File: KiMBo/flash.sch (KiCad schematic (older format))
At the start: 31 parts, among them IC1 24LC32AT-I/OT, U1 OSD3358, U5 74LVC1G06, U6 EMMC**G-S100

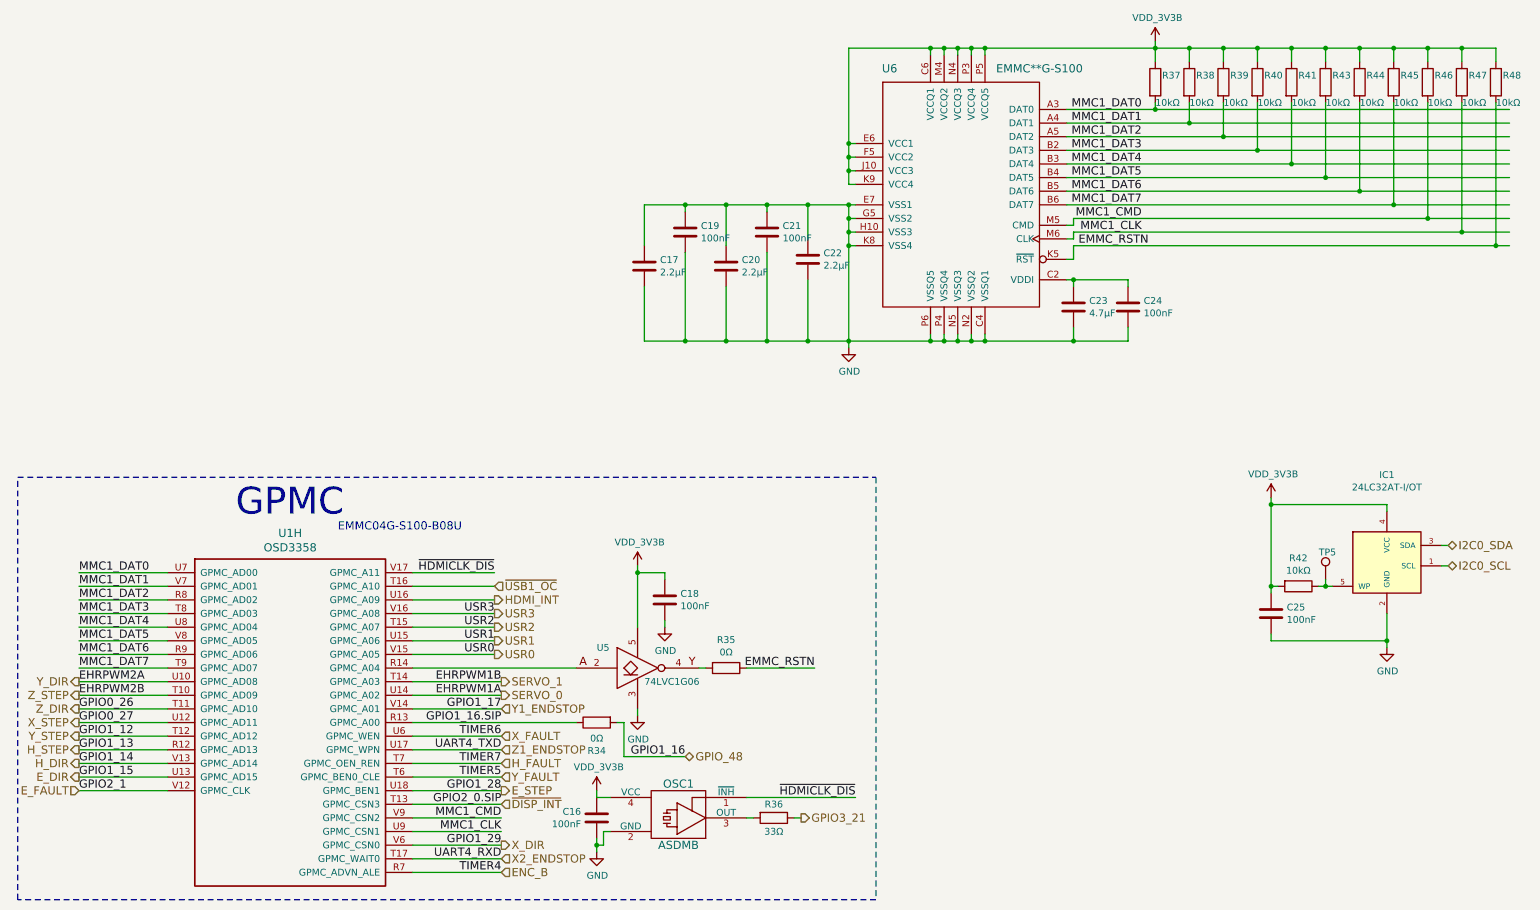
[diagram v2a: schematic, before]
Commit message: Use fixed 5V LM2592HV Buck, include SPI0 header for LCD
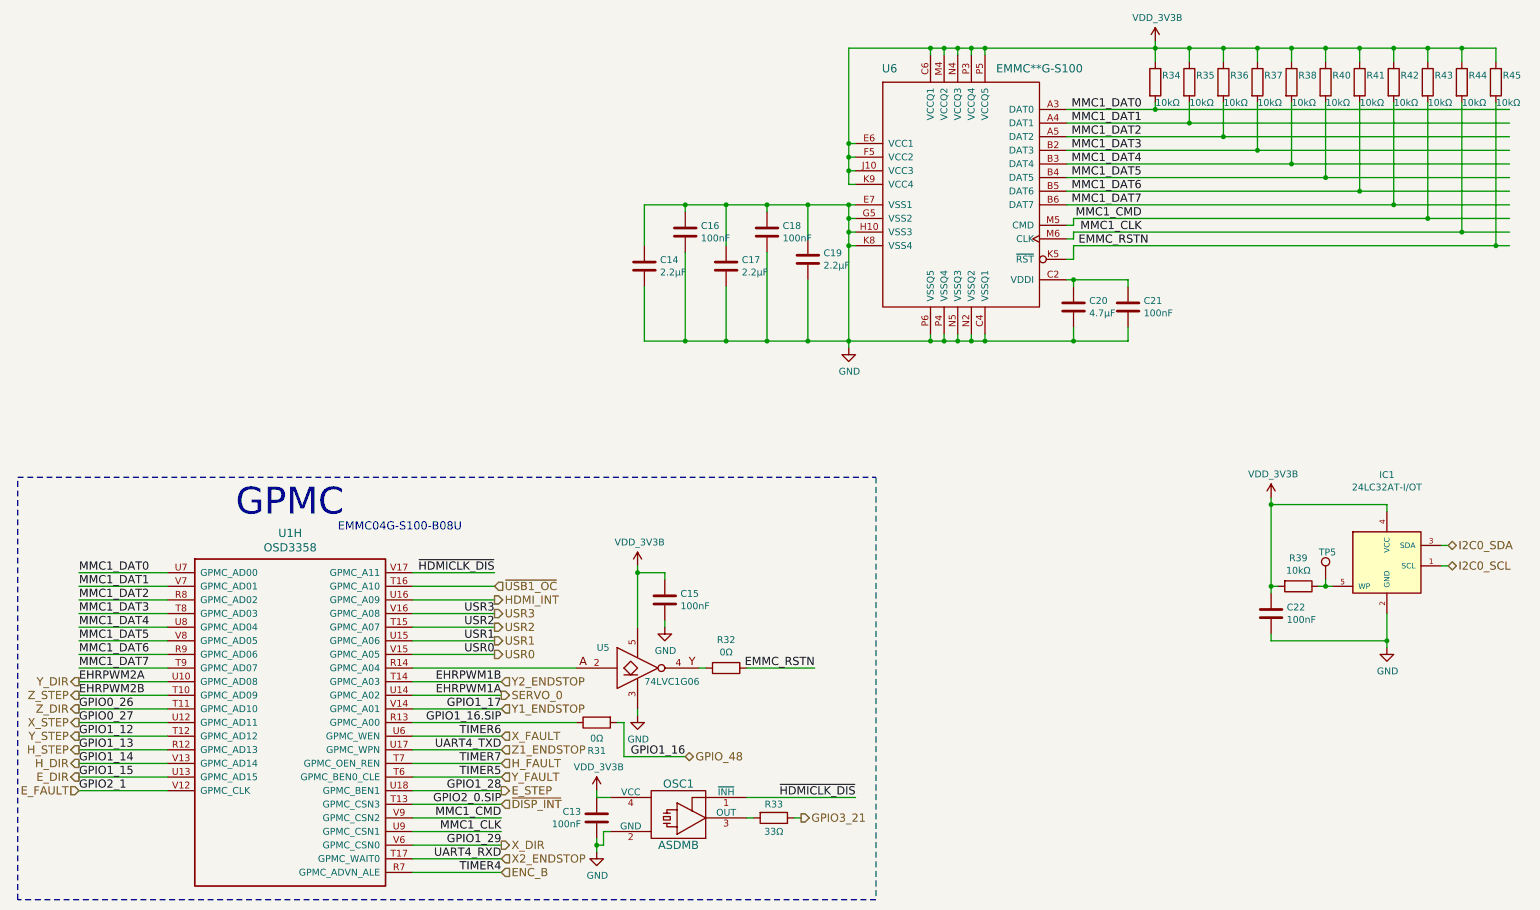
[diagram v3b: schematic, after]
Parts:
- renumbered C16 to C13, C17 to C14, C18 to C15, C19 to C16, C20 to C17, C21 to C18, C22 to C19, C23 to C20, C24 to C21, C25 to C22, R34 to R31, R35 to R32, R36 to R33, R37 to R34, R38 to R35, R39 to R36, R40 to R37, R41 to R38, R42 to R39, R43 to R40, R44 to R41, R45 to R42, R46 to R43, R47 to R44, R48 to R45
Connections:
- net labels added: Y2_ENDSTOP
- net labels removed: SERVO_1
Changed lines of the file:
@@
 $EndDescr
 $Comp
-L R R37
+L R R34
 U 1 1 58938DE0
 P 10550 2900
-F 0 "R37" H 10600 2950 50  0000 L CNN
+F 0 "R34" H 10600 2950 50  0000 L CNN
 F 1 "10kΩ" H 10550 2750 50  0000 L CNN
 F 2 "Resistors_SMD:R_0402" V 10480 2900 50  0001 C CNN
@@
 $EndComp
 $Comp
-L R R38
+L R R35
 U 1 1 58938E26
 P 10800 2900
-F 0 "R38" H 10850 2950 50  0000 L CNN
+F 0 "R35" H 10850 2950 50  0000 L CNN
 F 1 "10kΩ" H 10800 2750 50  0000 L CNN
 F 2 "Resistors_SMD:R_0402" V 10730 2900 50  0001 C CNN
@@
 $EndComp
 $Comp
-L R R39
+L R R36
 U 1 1 58938E51
 P 11050 2900
-F 0 "R39" H 11100 2950 50  0000 L CNN
+F 0 "R36" H 11100 2950 50  0000 L CNN
 F 1 "10kΩ" H 11050 2750 50  0000 L CNN
 F 2 "Resistors_SMD:R_0402" V 10980 2900 50  0001 C CNN
@@
 $EndComp
 $Comp
-L R R40
+L R R37
 U 1 1 58938E75
 P 11300 2900
-F 0 "R40" H 11350 2950 50  0000 L CNN
+F 0 "R37" H 11350 2950 50  0000 L CNN
 F 1 "10kΩ" H 11300 2750 50  0000 L CNN
 F 2 "Resistors_SMD:R_0402" V 11230 2900 50  0001 C CNN
@@
 $EndComp
 $Comp
-L R R41
+L R R38
 U 1 1 58938EA0
 P 11550 2900
-F 0 "R41" H 11600 2950 50  0000 L CNN
+F 0 "R38" H 11600 2950 50  0000 L CNN
 F 1 "10kΩ" H 11550 2750 50  0000 L CNN
 F 2 "Resistors_SMD:R_0402" V 11480 2900 50  0001 C CNN
@@
 $EndComp
 $Comp
-L R R43
+L R R40
 U 1 1 58938F20
 P 11800 2900
-F 0 "R43" H 11850 2950 50  0000 L CNN
+F 0 "R40" H 11850 2950 50  0000 L CNN
 F 1 "10kΩ" H 11800 2750 50  0000 L CNN
 F 2 "Resistors_SMD:R_0402" V 11730 2900 50  0001 C CNN
@@
 	9300 4800 9300 4750
 $Comp
-L R R44
+L R R41
 U 1 1 5893A6C3
 P 12050 2900
-F 0 "R44" H 12100 2950 50  0000 L CNN
+F 0 "R41" H 12100 2950 50  0000 L CNN
 F 1 "10kΩ" H 12050 2750 50  0000 L CNN
 F 2 "Resistors_SMD:R_0402" V 11980 2900 50  0001 C CNN
@@
 $EndComp
 $Comp
-L R R45
+L R R42
 U 1 1 5893A6FB
 P 12300 2900
-F 0 "R45" H 12350 2950 50  0000 L CNN
+F 0 "R42" H 12350 2950 50  0000 L CNN
 F 1 "10kΩ" H 12300 2750 50  0000 L CNN
 F 2 "Resistors_SMD:R_0402" V 12230 2900 50  0001 C CNN
@@
 $EndComp
 $Comp
-L R R46
+L R R43
 U 1 1 5893A736
 P 12550 2900
-F 0 "R46" H 12600 2950 50  0000 L CNN
+F 0 "R43" H 12600 2950 50  0000 L CNN
 F 1 "10kΩ" H 12550 2750 50  0000 L CNN
 F 2 "Resistors_SMD:R_0402" V 12480 2900 50  0001 C CNN
@@
 	10550 3100 10550 3050
 $Comp
-L R R47
+L R R44
 U 1 1 5893AC56
 P 12800 2900
-F 0 "R47" H 12850 2950 50  0000 L CNN
+F 0 "R44" H 12850 2950 50  0000 L CNN
 F 1 "10kΩ" H 12800 2750 50  0000 L CNN
 F 2 "Resistors_SMD:R_0402" V 12730 2900 50  0001 C CNN
@@
 $EndComp
 $Comp
-L R R48
+L R R45
 U 1 1 5893AC8F
 P 13050 2900
-F 0 "R48" H 13100 2950 50  0000 L CNN
+F 0 "R45" H 13100 2950 50  0000 L CNN
 F 1 "10kΩ" H 13050 2750 50  0000 L CNN
 F 2 "Resistors_SMD:R_0402" V 12980 2900 50  0001 C CNN
@@
 Connection ~ 12800 2650
 $Comp
-L GND #PWR097
+L GND #PWR092
 U 1 1 5893C2D6
 P 8300 4850
-F 0 "#PWR097" H 8300 4600 50  0001 C CNN
+F 0 "#PWR092" H 8300 4600 50  0001 C CNN
 F 1 "GND" H 8305 4677 50  0000 C CNN
 F 2 "" H 8300 4850 50  0000 C CNN
@@
 Connection ~ 8300 4800
 $Comp
-L C C23
+L C C20
 U 1 1 5893CB56
 P 9950 4550
-F 0 "C23" H 10065 4596 50  0000 L CNN
+F 0 "C20" H 10065 4596 50  0000 L CNN
 F 1 "4.7μF" H 10065 4505 50  0000 L CNN
 F 2 "Capacitors_SMD:C_0805" H 9950 4550 50  0001 C CNN
@@
 $EndComp
 $Comp
-L C C24
+L C C21
 U 1 1 5893CB95
 P 10350 4550
-F 0 "C24" H 10465 4596 50  0000 L CNN
+F 0 "C21" H 10465 4596 50  0000 L CNN
 F 1 "100nF" H 10465 4505 50  0000 L CNN
 F 2 "Capacitors_SMD:C_0402" H 10350 4550 50  0001 C CNN
@@
 Connection ~ 9950 4350
 $Comp
-L C C22
+L C C19
 U 1 1 5893CF89
 P 8000 4200
-F 0 "C22" H 8115 4246 50  0000 L CNN
+F 0 "C19" H 8115 4246 50  0000 L CNN
 F 1 "2.2μF" H 8115 4155 50  0000 L CNN
 F 2 "Capacitors_SMD:C_0805" H 8000 4200 50  0001 C CNN
@@
 $EndComp
 $Comp
-L C C21
+L C C18
 U 1 1 5893D253
 P 7700 4000
-F 0 "C21" H 7815 4046 50  0000 L CNN
+F 0 "C18" H 7815 4046 50  0000 L CNN
 F 1 "100nF" H 7815 3955 50  0000 L CNN
 F 2 "Capacitors_SMD:C_0402" H 7700 4000 50  0001 C CNN
@@
 $EndComp
 $Comp
-L C C20
+L C C17
 U 1 1 5893D333
 P 7400 4250
-F 0 "C20" H 7515 4296 50  0000 L CNN
+F 0 "C17" H 7515 4296 50  0000 L CNN
 F 1 "2.2μF" H 7515 4205 50  0000 L CNN
 F 2 "Capacitors_SMD:C_0805" H 7400 4250 50  0001 C CNN
@@
 $EndComp
 $Comp
-L C C19
+L C C16
 U 1 1 5893D48C
 P 7100 4000
-F 0 "C19" H 7215 4046 50  0000 L CNN
+F 0 "C16" H 7215 4046 50  0000 L CNN
 F 1 "100nF" H 7215 3955 50  0000 L CNN
 F 2 "Capacitors_SMD:C_0402" H 7100 4000 50  0001 C CNN
@@
 $EndComp
 $Comp
-L C C17
+L C C14
 U 1 1 5893D4EE
 P 6800 4250
-F 0 "C17" H 6915 4296 50  0000 L CNN
+F 0 "C14" H 6915 4296 50  0000 L CNN
 F 1 "2.2μF" H 6915 4205 50  0000 L CNN
 F 2 "Capacitors_SMD:C_0805" H 6800 4250 50  0001 C CNN
@@
 $EndComp
 $Comp
-L R R42
+L R R39
 U 1 1 589CA43D
 P 11600 6600
-F 0 "R42" V 11393 6600 50  0000 C CNN
+F 0 "R39" V 11393 6600 50  0000 C CNN
 F 1 "10kΩ" V 11484 6600 50  0000 C CNN
 F 2 "Resistors_SMD:R_0402" V 11530 6600 50  0001 C CNN
@@
 	11400 6600 11450 6600
 $Comp
-L C C25
+L C C22
 U 1 1 589CA9AC
 P 11400 6800
-F 0 "C25" H 11515 6846 50  0000 L CNN
+F 0 "C22" H 11515 6846 50  0000 L CNN
 F 1 "100nF" H 11515 6755 50  0000 L CNN
 F 2 "Capacitors_SMD:C_0402" H 11400 6800 50  0001 C CNN
@@
 	11400 7000 11400 6950
 $Comp
-L GND #PWR098
+L GND #PWR093
 U 1 1 589CAA98
 P 12250 7050
-F 0 "#PWR098" H 12250 6800 50  0001 C CNN
+F 0 "#PWR093" H 12250 6800 50  0001 C CNN
 F 1 "GND" H 12255 6877 50  0000 C CNN
 F 2 "" H 12250 7050 50  0000 C CNN
@@
 GPIO1_16.SIP
 $Comp
-L R R34
+L R R31
 U 1 1 58ED6392
 P 6450 7600
-F 0 "R34" V 6657 7600 50  0000 C CNN
+F 0 "R31" V 6657 7600 50  0000 C CNN
 F 1 "0Ω" V 6566 7600 50  0000 C CNN
 F 2 "Resistors_SMD:R_0402" V 6380 7600 50  0001 C CNN
@@
 $EndComp
 $Comp
-L GND #PWR099
+L GND #PWR094
 U 1 1 58ED63A5
 P 6750 7550
-F 0 "#PWR099" H 6750 7300 50  0001 C CNN
+F 0 "#PWR094" H 6750 7300 50  0001 C CNN
 F 1 "GND" H 6755 7377 50  0000 C CNN
 F 2 "" H 6750 7550 50  0000 C CNN
@@
 $EndComp
 $Comp
-L C C18
+L C C15
 U 1 1 58ED63B1
 P 6950 6700
-F 0 "C18" H 7065 6746 50  0000 L CNN
+F 0 "C15" H 7065 6746 50  0000 L CNN
 F 1 "100nF" H 7065 6655 50  0000 L CNN
 F 2 "Capacitors_SMD:C_0402" H 6988 6550 50  0001 C CNN
@@
 $EndComp
 $Comp
-L GND #PWR0100
+L GND #PWR095
 U 1 1 58ED63B8
 P 6950 6900
-F 0 "#PWR0100" H 6950 6650 50  0001 C CNN
+F 0 "#PWR095" H 6950 6650 50  0001 C CNN
 F 1 "GND" H 6955 6727 50  0000 C CNN
 F 2 "" H 6950 6900 50  0000 C CNN
@@
 $EndComp
 $Comp
-L R R35
+L R R32
 U 1 1 58ED63BE
 P 7400 7200
-F 0 "R35" V 7193 7200 50  0000 C CNN
+F 0 "R32" V 7193 7200 50  0000 C CNN
 F 1 "0Ω" V 7284 7200 50  0000 C CNN
 F 2 "Resistors_SMD:R_0402" V 7330 7200 50  0001 C CNN
@@
 $EndComp
 $Comp
-L C C16
+L C C13
 U 1 1 58ED63CD
 P 6450 8300
-F 0 "C16" H 6565 8346 50  0000 L CNN
+F 0 "C13" H 6565 8346 50  0000 L CNN
 F 1 "100nF" H 6565 8255 50  0000 L CNN
 F 2 "Capacitors_SMD:C_0402" H 6450 8300 50  0001 C CNN
@@
 $EndComp
 $Comp
-L GND #PWR0101
+L GND #PWR096
 U 1 1 58ED63D4
 P 6450 8550
-F 0 "#PWR0101" H 6450 8300 50  0001 C CNN
+F 0 "#PWR096" H 6450 8300 50  0001 C CNN
 F 1 "GND" H 6455 8377 50  0000 C CNN
 F 2 "" H 6450 8550 50  0000 C CNN
@@
 $EndComp
 $Comp
-L R R36
+L R R33
 U 1 1 58ED63E0
 P 7750 8300
-F 0 "R36" V 7650 8300 50  0000 C CNN
+F 0 "R33" V 7650 8300 50  0000 C CNN
 F 1 "33Ω" V 7850 8300 50  0000 C CNN
 F 2 "" V 7680 8300 50  0001 C CNN
@@
 Text HLabel 7950 8300 2    60   Output ~ 0
 GPIO3_21
-Text HLabel 5750 7300 2    60   Output ~ 0
-SERVO_1
 Text HLabel 5750 7400 2    60   Output ~ 0
 SERVO_0
 $Comp
-L VDD_3V3B #PWR0102
+L VDD_3V3B #PWR097
 U 1 1 59E9BAE0
 P 10550 2600
-F 0 "#PWR0102" H 10550 2450 50  0001 C CNN
+F 0 "#PWR097" H 10550 2450 50  0001 C CNN
 F 1 "VDD_3V3B" H 10565 2773 50  0000 C CNN
 F 2 "" H 10550 2600 50  0000 C CNN
@@
 USR0
 $Comp
-L VDD_3V3B #PWR0103
+L VDD_3V3B #PWR098
 U 1 1 59FAFB00
 P 6450 8100
-F 0 "#PWR0103" H 6450 7950 50  0001 C CNN
+F 0 "#PWR098" H 6450 7950 50  0001 C CNN
 F 1 "VDD_3V3B" H 6465 8273 50  0000 C CNN
 F 2 "" H 6450 8100 50  0000 C CNN
@@
 $EndComp
 $Comp
-L VDD_3V3B #PWR0104
+L VDD_3V3B #PWR099
 U 1 1 59FBC4DE
 P 6750 6450
-F 0 "#PWR0104" H 6750 6300 50  0001 C CNN
+F 0 "#PWR099" H 6750 6300 50  0001 C CNN
 F 1 "VDD_3V3B" H 6765 6623 50  0000 C CNN
 F 2 "" H 6750 6450 50  0000 C CNN
@@
 Connection ~ 11400 6600
 $Comp
-L VDD_3V3B #PWR0105
+L VDD_3V3B #PWR0100
 U 1 1 59FBD7EE
 P 11400 5950
-F 0 "#PWR0105" H 11400 5800 50  0001 C CNN
+F 0 "#PWR0100" H 11400 5800 50  0001 C CNN
 F 1 "VDD_3V3B" H 11415 6123 50  0000 C CNN
 F 2 "" H 11400 5950 50  0000 C CNN
@@
 Text HLabel 5750 8200 2    60   Input ~ 0
 ~DISP_INT
+Text HLabel 5750 7300 2    60   Input ~ 0
+Y2_ENDSTOP
 $EndSCHEMATC

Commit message: Assocate more footprints
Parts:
- C13, C15, C16, C18, C21, C22: footprint Capacitors_SMD:C_0402 -> Capacitors_SMD:C_0603
- R31, R32, R34, R35, R36, R37, R38, R39, R40, R41, R42, R43, R44, R45: footprint Resistors_SMD:R_0402 -> Resistors_SMD:R_0603
- R33: footprint (none) -> Resistors_SMD:R_0603
- U1: footprint (none) -> KiMBo:BGA-400-1-27mm
- U6: footprint (none) -> KiMBo:EMMCxxG-S100
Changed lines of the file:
@@
 F 0 "R34" H 10600 2950 50  0000 L CNN
 F 1 "10kΩ" H 10550 2750 50  0000 L CNN
-F 2 "Resistors_SMD:R_0402" V 10480 2900 50  0001 C CNN
+F 2 "Resistors_SMD:R_0603" V 10480 2900 50  0001 C CNN
 F 3 "" H 10550 2900 50  0000 C CNN
 	1    10550 2900
@@
 F 0 "R35" H 10850 2950 50  0000 L CNN
 F 1 "10kΩ" H 10800 2750 50  0000 L CNN
-F 2 "Resistors_SMD:R_0402" V 10730 2900 50  0001 C CNN
+F 2 "Resistors_SMD:R_0603" V 10730 2900 50  0001 C CNN
 F 3 "" H 10800 2900 50  0000 C CNN
 	1    10800 2900
@@
 F 0 "R36" H 11100 2950 50  0000 L CNN
 F 1 "10kΩ" H 11050 2750 50  0000 L CNN
-F 2 "Resistors_SMD:R_0402" V 10980 2900 50  0001 C CNN
+F 2 "Resistors_SMD:R_0603" V 10980 2900 50  0001 C CNN
 F 3 "" H 11050 2900 50  0000 C CNN
 	1    11050 2900
@@
 F 0 "R37" H 11350 2950 50  0000 L CNN
 F 1 "10kΩ" H 11300 2750 50  0000 L CNN
-F 2 "Resistors_SMD:R_0402" V 11230 2900 50  0001 C CNN
+F 2 "Resistors_SMD:R_0603" V 11230 2900 50  0001 C CNN
 F 3 "" H 11300 2900 50  0000 C CNN
 	1    11300 2900
@@
 F 0 "R38" H 11600 2950 50  0000 L CNN
 F 1 "10kΩ" H 11550 2750 50  0000 L CNN
-F 2 "Resistors_SMD:R_0402" V 11480 2900 50  0001 C CNN
+F 2 "Resistors_SMD:R_0603" V 11480 2900 50  0001 C CNN
 F 3 "" H 11550 2900 50  0000 C CNN
 	1    11550 2900
@@
 F 0 "R40" H 11850 2950 50  0000 L CNN
 F 1 "10kΩ" H 11800 2750 50  0000 L CNN
-F 2 "Resistors_SMD:R_0402" V 11730 2900 50  0001 C CNN
+F 2 "Resistors_SMD:R_0603" V 11730 2900 50  0001 C CNN
 F 3 "" H 11800 2900 50  0000 C CNN
 	1    11800 2900
@@
 F 0 "R41" H 12100 2950 50  0000 L CNN
 F 1 "10kΩ" H 12050 2750 50  0000 L CNN
-F 2 "Resistors_SMD:R_0402" V 11980 2900 50  0001 C CNN
+F 2 "Resistors_SMD:R_0603" V 11980 2900 50  0001 C CNN
 F 3 "" H 12050 2900 50  0000 C CNN
 	1    12050 2900
@@
 F 0 "R42" H 12350 2950 50  0000 L CNN
 F 1 "10kΩ" H 12300 2750 50  0000 L CNN
-F 2 "Resistors_SMD:R_0402" V 12230 2900 50  0001 C CNN
+F 2 "Resistors_SMD:R_0603" V 12230 2900 50  0001 C CNN
 F 3 "" H 12300 2900 50  0000 C CNN
 	1    12300 2900
@@
 F 0 "R43" H 12600 2950 50  0000 L CNN
 F 1 "10kΩ" H 12550 2750 50  0000 L CNN
-F 2 "Resistors_SMD:R_0402" V 12480 2900 50  0001 C CNN
+F 2 "Resistors_SMD:R_0603" V 12480 2900 50  0001 C CNN
 F 3 "" H 12550 2900 50  0000 C CNN
 	1    12550 2900
@@
 F 0 "R44" H 12850 2950 50  0000 L CNN
 F 1 "10kΩ" H 12800 2750 50  0000 L CNN
-F 2 "Resistors_SMD:R_0402" V 12730 2900 50  0001 C CNN
+F 2 "Resistors_SMD:R_0603" V 12730 2900 50  0001 C CNN
 F 3 "" H 12800 2900 50  0000 C CNN
 	1    12800 2900
@@
 F 0 "R45" H 13100 2950 50  0000 L CNN
 F 1 "10kΩ" H 13050 2750 50  0000 L CNN
-F 2 "Resistors_SMD:R_0402" V 12980 2900 50  0001 C CNN
+F 2 "Resistors_SMD:R_0603" V 12980 2900 50  0001 C CNN
 F 3 "" H 13050 2900 50  0000 C CNN
 	1    13050 2900
@@
 F 0 "C21" H 10465 4596 50  0000 L CNN
 F 1 "100nF" H 10465 4505 50  0000 L CNN
-F 2 "Capacitors_SMD:C_0402" H 10350 4550 50  0001 C CNN
+F 2 "Capacitors_SMD:C_0603" H 10350 4550 50  0001 C CNN
 F 3 "" H 10350 4550 50  0000 C CNN
 	1    10350 4550
@@
 F 0 "C18" H 7815 4046 50  0000 L CNN
 F 1 "100nF" H 7815 3955 50  0000 L CNN
-F 2 "Capacitors_SMD:C_0402" H 7700 4000 50  0001 C CNN
+F 2 "Capacitors_SMD:C_0603" H 7700 4000 50  0001 C CNN
 F 3 "" H 7700 4000 50  0000 C CNN
 	1    7700 4000
@@
 F 0 "C16" H 7215 4046 50  0000 L CNN
 F 1 "100nF" H 7215 3955 50  0000 L CNN
-F 2 "Capacitors_SMD:C_0402" H 7100 4000 50  0001 C CNN
+F 2 "Capacitors_SMD:C_0603" H 7100 4000 50  0001 C CNN
 F 3 "" H 7100 4000 50  0000 C CNN
 	1    7100 4000
@@
 F 0 "R39" V 11393 6600 50  0000 C CNN
 F 1 "10kΩ" V 11484 6600 50  0000 C CNN
-F 2 "Resistors_SMD:R_0402" V 11530 6600 50  0001 C CNN
+F 2 "Resistors_SMD:R_0603" V 11530 6600 50  0001 C CNN
 F 3 "" H 11600 6600 50  0000 C CNN
 	1    11600 6600
@@
 F 0 "C22" H 11515 6846 50  0000 L CNN
 F 1 "100nF" H 11515 6755 50  0000 L CNN
-F 2 "Capacitors_SMD:C_0402" H 11400 6800 50  0001 C CNN
+F 2 "Capacitors_SMD:C_0603" H 11400 6800 50  0001 C CNN
 F 3 "" H 11400 6800 50  0000 C CNN
 	1    11400 6800
@@
 F 0 "U1" H 4200 6790 60  0000 C CNN
 F 1 "OSD3358" H 4200 6684 60  0000 C CNN
-F 2 "" H 3300 6500 60  0001 C CNN
+F 2 "KiMBo:BGA-400-1-27mm" H 3300 6500 60  0001 C CNN
 F 3 "" H 3300 6500 60  0001 C CNN
 	8    3300 6500
@@
 F 0 "R31" V 6657 7600 50  0000 C CNN
 F 1 "0Ω" V 6566 7600 50  0000 C CNN
-F 2 "Resistors_SMD:R_0402" V 6380 7600 50  0001 C CNN
+F 2 "Resistors_SMD:R_0603" V 6380 7600 50  0001 C CNN
 F 3 "" H 6450 7600 50  0000 C CNN
 	1    6450 7600
@@
 F 0 "C15" H 7065 6746 50  0000 L CNN
 F 1 "100nF" H 7065 6655 50  0000 L CNN
-F 2 "Capacitors_SMD:C_0402" H 6988 6550 50  0001 C CNN
+F 2 "Capacitors_SMD:C_0603" H 6988 6550 50  0001 C CNN
 F 3 "" H 6950 6700 50  0000 C CNN
 	1    6950 6700
@@
 F 0 "R32" V 7193 7200 50  0000 C CNN
 F 1 "0Ω" V 7284 7200 50  0000 C CNN
-F 2 "Resistors_SMD:R_0402" V 7330 7200 50  0001 C CNN
+F 2 "Resistors_SMD:R_0603" V 7330 7200 50  0001 C CNN
 F 3 "" H 7400 7200 50  0000 C CNN
 	1    7400 7200
@@
 F 0 "C13" H 6565 8346 50  0000 L CNN
 F 1 "100nF" H 6565 8255 50  0000 L CNN
-F 2 "Capacitors_SMD:C_0402" H 6450 8300 50  0001 C CNN
+F 2 "Capacitors_SMD:C_0603" H 6450 8300 50  0001 C CNN
 F 3 "" H 6450 8300 50  0000 C CNN
 	1    6450 8300
@@
 F 0 "R33" V 7650 8300 50  0000 C CNN
 F 1 "33Ω" V 7850 8300 50  0000 C CNN
-F 2 "" V 7680 8300 50  0001 C CNN
+F 2 "Resistors_SMD:R_0603" V 7680 8300 50  0001 C CNN
 F 3 "" H 7750 8300 50  0000 C CNN
 	1    7750 8300
@@
 F 0 "U6" H 8600 4700 60  0000 C CNN
 F 1 "EMMC**G-S100" H 9700 4700 60  0000 C CNN
-F 2 "" H 9150 4250 60  0001 C CNN
+F 2 "KiMBo:EMMCxxG-S100" H 9150 4250 60  0001 C CNN
 F 3 "" H 9150 4250 60  0001 C CNN
 	1    9150 3750
